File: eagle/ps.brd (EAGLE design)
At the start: 122.7 x 94.2 mm, 12 parts, among them J1 PIN2F061.100, J2 PIN2F061.100

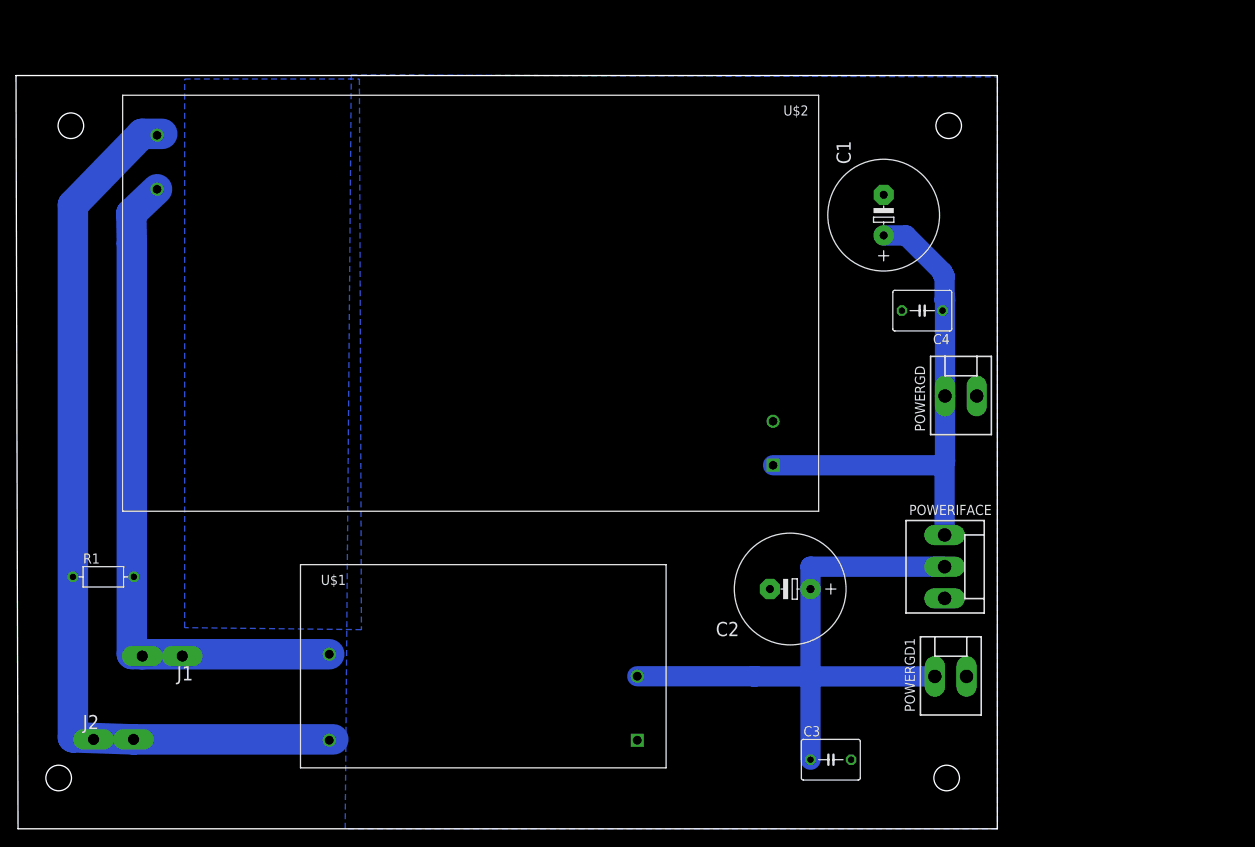
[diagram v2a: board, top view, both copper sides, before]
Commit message: tweaks. still need bigger vias for zeners and hv resistors
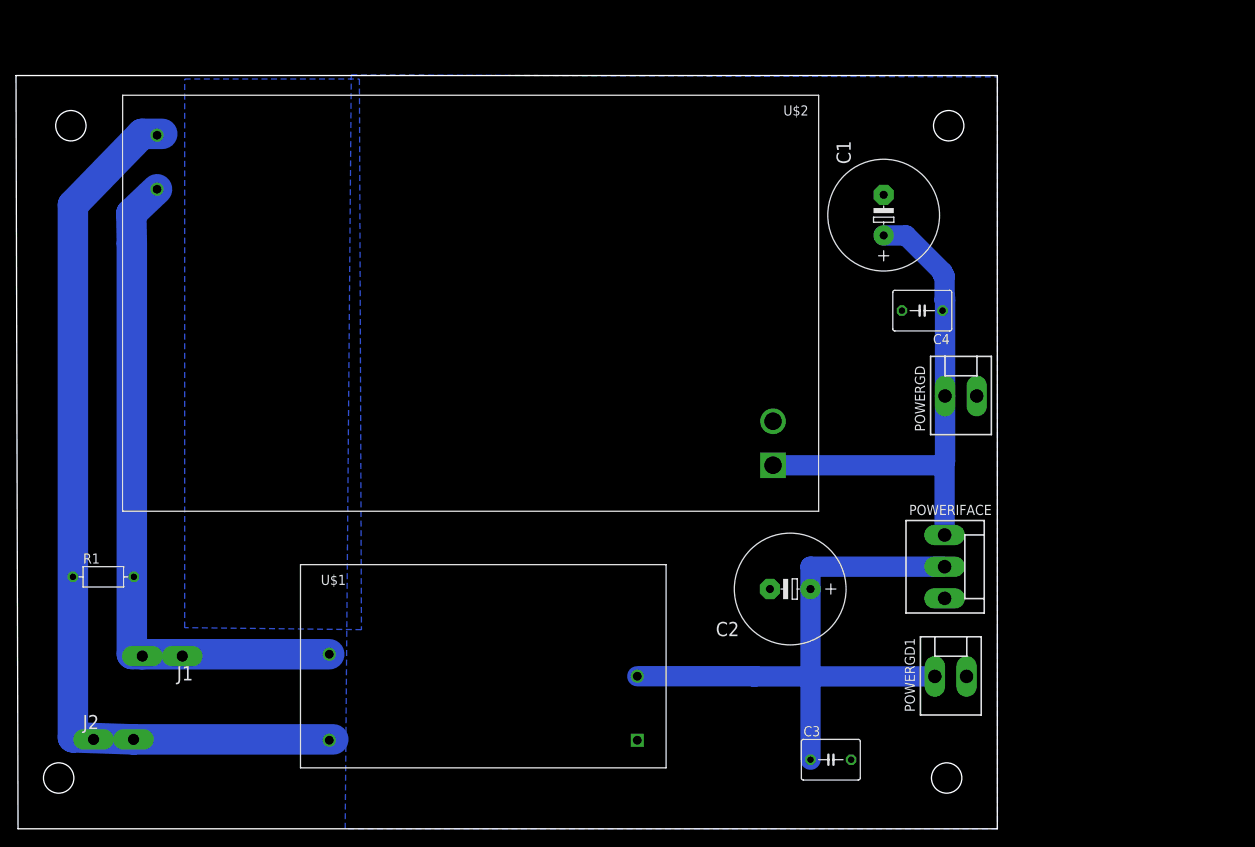
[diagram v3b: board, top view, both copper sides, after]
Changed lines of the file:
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@@
 <grid distance="0.01" unitdist="inch" unit="inch" style="lines" multiple="1" display="no" altdistance="0.025" altunitdist="inch" altunit="inch"/>
 <layers>
-<layer number="1" name="Top" color="4" fill="1" visible="yes" active="yes"/>
+<layer number="1" name="Top" color="4" fill="1" visible="no" active="yes"/>
 <layer number="2" name="Route2" color="1" fill="3" visible="no" active="no"/>
 <layer number="3" name="Route3" color="4" fill="3" visible="no" active="no"/>
@@
 <layer number="17" name="Pads" color="2" fill="1" visible="yes" active="yes"/>
 <layer number="18" name="Vias" color="2" fill="1" visible="yes" active="yes"/>
-<layer number="19" name="Unrouted" color="6" fill="1" visible="yes" active="yes"/>
+<layer number="19" name="Unrouted" color="6" fill="1" visible="no" active="yes"/>
 <layer number="20" name="Dimension" color="15" fill="1" visible="yes" active="yes"/>
-<layer number="21" name="tPlace" color="7" fill="1" visible="yes" active="yes"/>
-<layer number="22" name="bPlace" color="7" fill="1" visible="yes" active="yes"/>
-<layer number="23" name="tOrigins" color="15" fill="1" visible="yes" active="yes"/>
-<layer number="24" name="bOrigins" color="15" fill="1" visible="yes" active="yes"/>
-<layer number="25" name="tNames" color="7" fill="1" visible="yes" active="yes"/>
-<layer number="26" name="bNames" color="7" fill="1" visible="yes" active="yes"/>
-<layer number="27" name="tValues" color="7" fill="1" visible="yes" active="yes"/>
-<layer number="28" name="bValues" color="7" fill="1" visible="yes" active="yes"/>
-<layer number="29" name="tStop" color="7" fill="3" visible="yes" active="yes"/>
-<layer number="30" name="bStop" color="7" fill="6" visible="yes" active="yes"/>
-<layer number="31" name="tCream" color="7" fill="4" visible="yes" active="yes"/>
-<layer number="32" name="bCream" color="7" fill="5" visible="yes" active="yes"/>
-<layer number="33" name="tFinish" color="6" fill="3" visible="yes" active="yes"/>
-<layer number="34" name="bFinish" color="6" fill="6" visible="yes" active="yes"/>
-<layer number="35" name="tGlue" color="7" fill="4" visible="yes" active="yes"/>
-<layer number="36" name="bGlue" color="7" fill="5" visible="yes" active="yes"/>
-<layer number="37" name="tTest" color="7" fill="1" visible="yes" active="yes"/>
-<layer number="38" name="bTest" color="7" fill="1" visible="yes" active="yes"/>
-<layer number="39" name="tKeepout" color="4" fill="11" visible="yes" active="yes"/>
-<layer number="40" name="bKeepout" color="1" fill="11" visible="yes" active="yes"/>
-<layer number="41" name="tRestrict" color="4" fill="10" visible="yes" active="yes"/>
-<layer number="42" name="bRestrict" color="1" fill="10" visible="yes" active="yes"/>
-<layer number="43" name="vRestrict" color="2" fill="10" visible="yes" active="yes"/>
-<layer number="44" name="Drills" color="7" fill="1" visible="yes" active="yes"/>
-<layer number="45" name="Holes" color="7" fill="1" visible="yes" active="yes"/>
-<layer number="46" name="Milling" color="3" fill="1" visible="yes" active="yes"/>
-<layer number="47" name="Measures" color="7" fill="1" visible="yes" active="yes"/>
-<layer number="48" name="Document" color="7" fill="1" visible="yes" active="yes"/>
-<layer number="49" name="Reference" color="7" fill="1" visible="yes" active="yes"/>
-<layer number="51" name="tDocu" color="7" fill="1" visible="yes" active="yes"/>
-<layer number="52" name="bDocu" color="7" fill="1" visible="yes" active="yes"/>
+<layer number="21" name="tPlace" color="7" fill="1" visible="no" active="yes"/>
+<layer number="22" name="bPlace" color="7" fill="1" visible="no" active="yes"/>
+<layer number="23" name="tOrigins" color="15" fill="1" visible="no" active="yes"/>
+<layer number="24" name="bOrigins" color="15" fill="1" visible="no" active="yes"/>
+<layer number="25" name="tNames" color="7" fill="1" visible="no" active="yes"/>
+<layer number="26" name="bNames" color="7" fill="1" visible="no" active="yes"/>
+<layer number="27" name="tValues" color="7" fill="1" visible="no" active="yes"/>
+<layer number="28" name="bValues" color="7" fill="1" visible="no" active="yes"/>
+<layer number="29" name="tStop" color="7" fill="3" visible="no" active="yes"/>
+<layer number="30" name="bStop" color="7" fill="6" visible="no" active="yes"/>
+<layer number="31" name="tCream" color="7" fill="4" visible="no" active="yes"/>
+<layer number="32" name="bCream" color="7" fill="5" visible="no" active="yes"/>
+<layer number="33" name="tFinish" color="6" fill="3" visible="no" active="yes"/>
+<layer number="34" name="bFinish" color="6" fill="6" visible="no" active="yes"/>
+<layer number="35" name="tGlue" color="7" fill="4" visible="no" active="yes"/>
+<layer number="36" name="bGlue" color="7" fill="5" visible="no" active="yes"/>
+<layer number="37" name="tTest" color="7" fill="1" visible="no" active="yes"/>
+<layer number="38" name="bTest" color="7" fill="1" visible="no" active="yes"/>
+<layer number="39" name="tKeepout" color="4" fill="11" visible="no" active="yes"/>
+<layer number="40" name="bKeepout" color="1" fill="11" visible="no" active="yes"/>
+<layer number="41" name="tRestrict" color="4" fill="10" visible="no" active="yes"/>
+<layer number="42" name="bRestrict" color="1" fill="10" visible="no" active="yes"/>
+<layer number="43" name="vRestrict" color="2" fill="10" visible="no" active="yes"/>
+<layer number="44" name="Drills" color="7" fill="1" visible="no" active="yes"/>
+<layer number="45" name="Holes" color="7" fill="1" visible="no" active="yes"/>
+<layer number="46" name="Milling" color="3" fill="1" visible="no" active="yes"/>
+<layer number="47" name="Measures" color="7" fill="1" visible="no" active="yes"/>
+<layer number="48" name="Document" color="7" fill="1" visible="no" active="yes"/>
+<layer number="49" name="Reference" color="7" fill="1" visible="no" active="yes"/>
+<layer number="51" name="tDocu" color="7" fill="1" visible="no" active="yes"/>
+<layer number="52" name="bDocu" color="7" fill="1" visible="no" active="yes"/>
 <layer number="90" name="Modules" color="5" fill="1" visible="no" active="no"/>
 <layer number="91" name="Nets" color="2" fill="1" visible="no" active="no"/>
@@
 <wire x1="122.154" y1="93.904" x2="-0.508" y2="93.904" width="0" layer="20"/>
 <wire x1="-0.508" y1="93.904" x2="-0.254" y2="-0.254" width="0" layer="20"/>
-<hole x="116.078" y="87.63" drill="3.2"/>
-<hole x="115.824" y="6.096" drill="3.2"/>
-<hole x="6.35" y="87.63" drill="3.2"/>
-<hole x="4.826" y="6.096" drill="3.2"/>
+<hole x="116.078" y="87.63" drill="3.7973"/>
+<hole x="115.824" y="6.096" drill="3.7973"/>
+<hole x="6.35" y="87.63" drill="3.7973"/>
+<hole x="4.826" y="6.096" drill="3.7973"/>
 </plain>
 <attributes>
